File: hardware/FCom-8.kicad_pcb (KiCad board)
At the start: 2 copper layers, 94 x 127 mm, 53 parts, among them J101 USB_C_Receptacle_USB2.0_14P, SW101 SW_DIP_x08, SW102 SW_DIP_x08, SW103 SW_Push_Dual, SW104 SW_DIP_x04, U101 65C02, U102 AS6C1008-55PCN, U103 65C22, U104 74HC245, U105 74HC245, U106 74HC04, U107 74LS08, U108 74LS08, U109 74LS21, U110 MCP23S17_SP

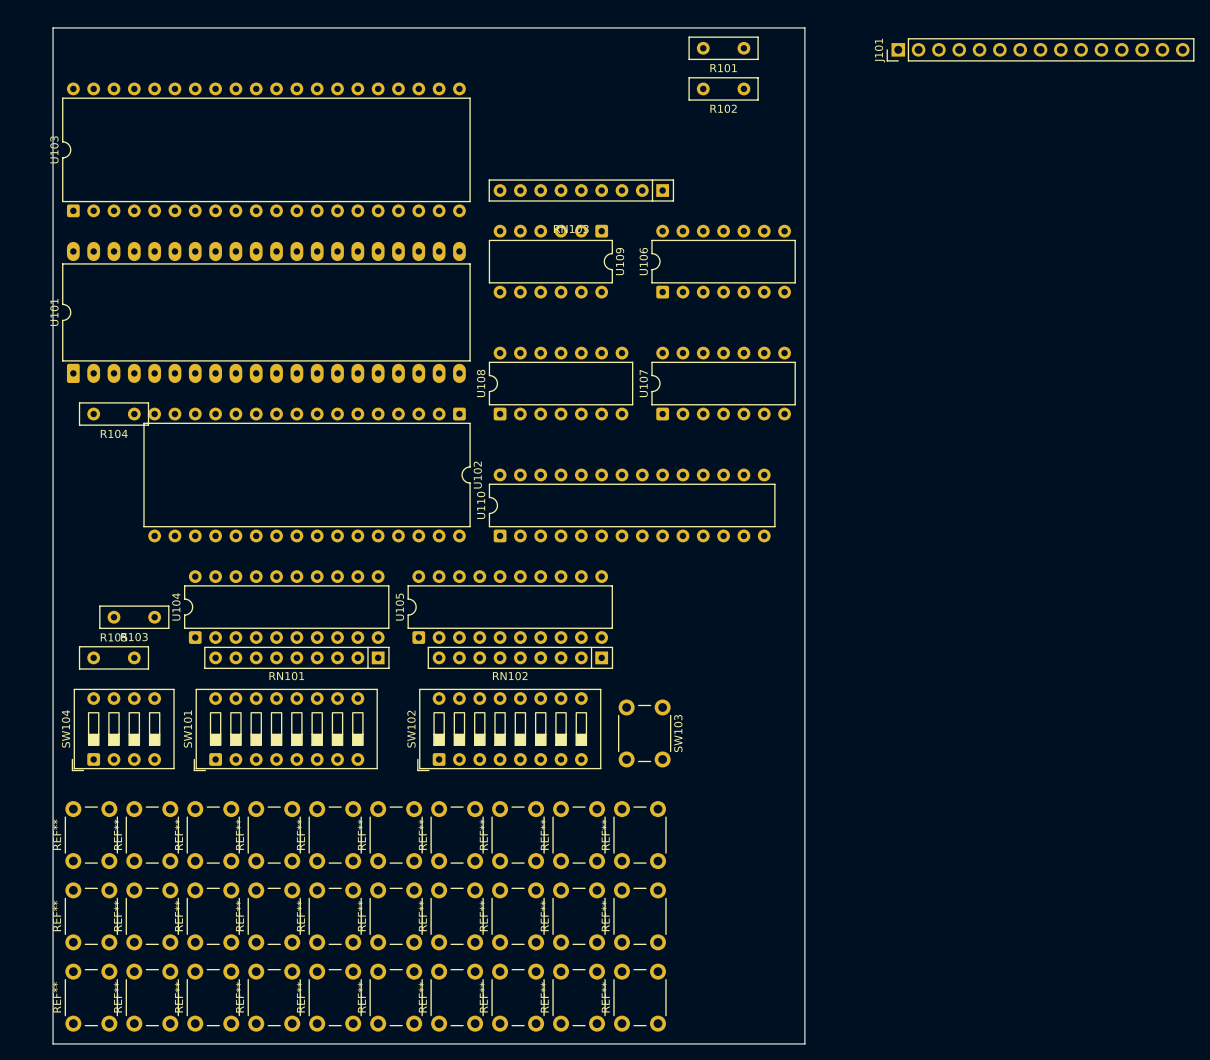
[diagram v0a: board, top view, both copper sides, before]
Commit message: Complete schematics and component placements on board
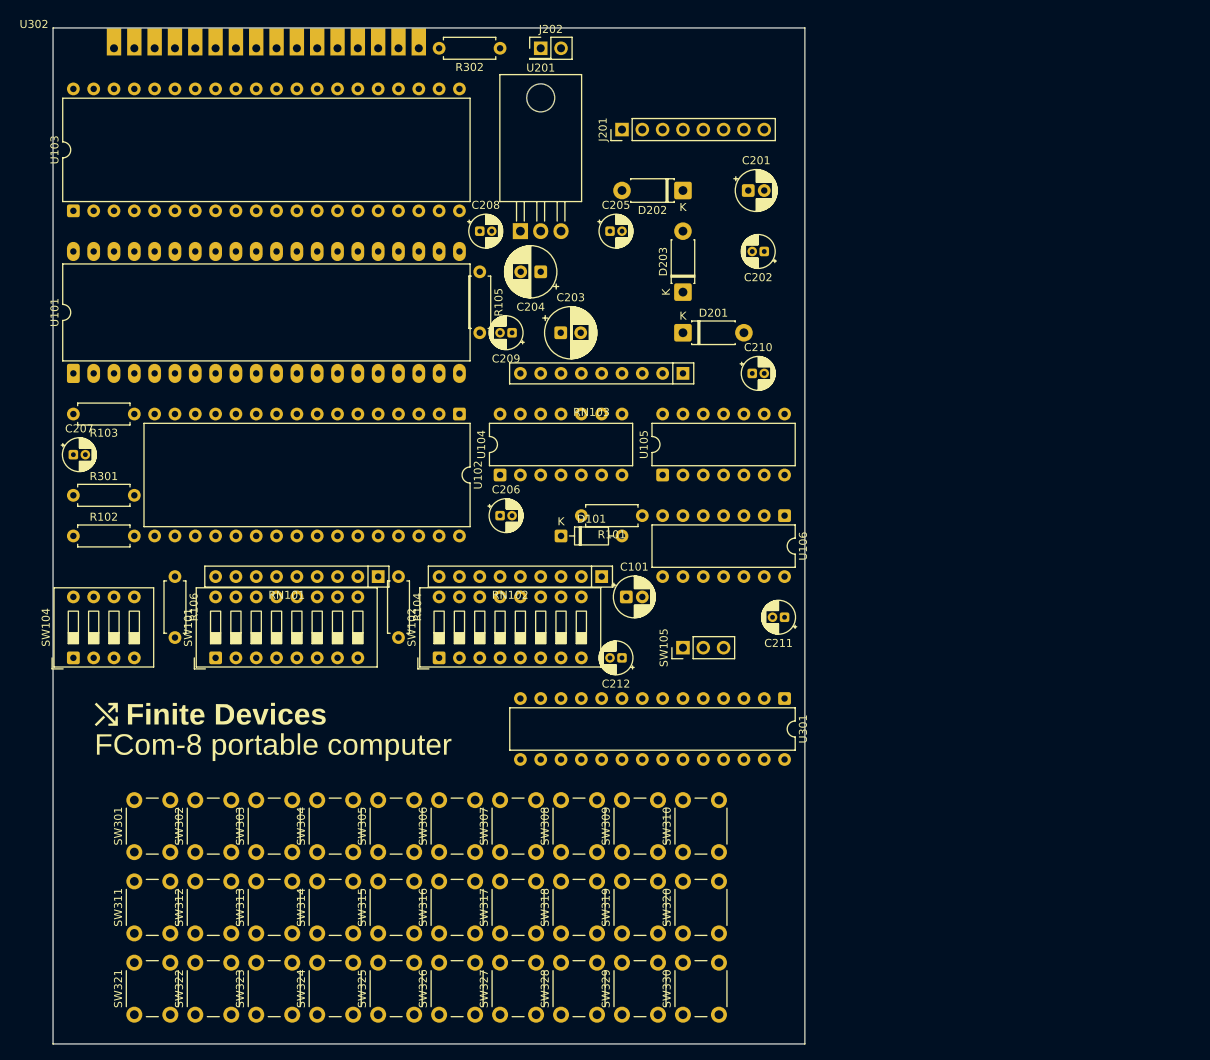
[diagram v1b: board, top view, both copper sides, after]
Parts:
- removed J101: USB_C_Receptacle_USB2.0_14P, Connector_PinHeader_2.54mm:PinHeader_1x15_P2.54mm_Vertical
- removed the R102 at (137.2, 33.0)
- removed the R103 at (63.5, 99.1)
- removed REF** (x30): SW_PUSH_6mm, Button_Switch_THT:SW_PUSH_6mm
- removed SW103: SW_Push_Dual, Button_Switch_THT:SW_PUSH_6mm_H5mm
- removed U107, U108: 74LS08, Package_DIP:DIP-14_W7.62mm
- removed U109: 74LS21, Package_DIP:DIP-12_W7.62mm
- removed U110: MCP23S17_SP, Package_DIP:DIP-28_W7.62mm
- added C101: 4.7u, Capacitor_THT:CP_Radial_D5.0mm_P2.00mm, F.Cu at (122.5, 96.5)
- added C201: 10u, Capacitor_THT:CP_Radial_D5.0mm_P2.00mm, F.Cu at (137.7, 45.7)
- added C202: 0.1u, Capacitor_THT:CP_Radial_D4.0mm_P1.50mm, F.Cu at (139.7, 53.3)
- added C203: 100u, Capacitor_THT:CP_Radial_D6.3mm_P2.50mm, F.Cu at (114.3, 63.5)
- added C204: 100u, Capacitor_THT:CP_Radial_D6.3mm_P2.50mm, F.Cu at (111.8, 55.9)
- added C205: 0.1u, Capacitor_THT:CP_Radial_D4.0mm_P1.50mm, F.Cu at (120.4, 50.8)
- added C206: 0.1u, Capacitor_THT:CP_Radial_D4.0mm_P1.50mm, F.Cu at (106.7, 86.4)
- added C207: 0.1u, Capacitor_THT:CP_Radial_D4.0mm_P1.50mm, F.Cu at (53.3, 78.7)
- added C208: 0.1u, Capacitor_THT:CP_Radial_D4.0mm_P1.50mm, F.Cu at (104.1, 50.8)
- added C209: 0.1u, Capacitor_THT:CP_Radial_D4.0mm_P1.50mm, F.Cu at (108.2, 63.5)
- added C210: 0.1u, Capacitor_THT:CP_Radial_D4.0mm_P1.50mm, F.Cu at (138.2, 68.6)
- added C211: 0.1u, Capacitor_THT:CP_Radial_D4.0mm_P1.50mm, F.Cu at (142.2, 99.1)
- added C212: 0.1u, Capacitor_THT:CP_Radial_D4.0mm_P1.50mm, F.Cu at (121.9, 104.1)
- added D101: 1N4148, Diode_THT:D_DO-35_SOD27_P7.62mm_Horizontal, F.Cu at (114.3, 88.9)
- added D201: D_Schottky, Diode_THT:D_DO-41_SOD81_P7.62mm_Horizontal, F.Cu at (129.5, 63.5)
- added D202: D_Schottky, Diode_THT:D_DO-41_SOD81_P7.62mm_Horizontal, F.Cu at (129.5, 45.7)
- added D203: D_Schottky, Diode_THT:D_DO-41_SOD81_P7.62mm_Horizontal, F.Cu at (129.5, 58.4)
- added G***: LOGO, Components:Badge, F.Cu at (78.7, 113.0)
- added J201: 4090 USB-C, Connector_PinHeader_2.54mm:PinHeader_1x08_P2.54mm_Vertical, F.Cu at (121.9, 38.1)
- added J202: 9V battery, Connector_PinHeader_2.54mm:PinHeader_2x01_P2.54mm_Vertical, F.Cu at (111.8, 27.9)
- added R104: 10k, Resistor_THT:R_Axial_DIN0207_L6.3mm_D2.5mm_P7.62mm_Horizontal, F.Cu at (94.0, 94.0)
- added R105: 10k, Resistor_THT:R_Axial_DIN0207_L6.3mm_D2.5mm_P7.62mm_Horizontal, F.Cu at (104.1, 55.9)
- added R106: 10k, Resistor_THT:R_Axial_DIN0207_L6.3mm_D2.5mm_P7.62mm_Horizontal, F.Cu at (66.0, 94.0)
- added R301: 10k, Resistor_THT:R_Axial_DIN0207_L6.3mm_D2.5mm_P7.62mm_Horizontal, F.Cu at (53.3, 83.8)
- added R302: 1.2k, Resistor_THT:R_Axial_DIN0207_L6.3mm_D2.5mm_P7.62mm_Horizontal, F.Cu at (106.7, 27.9)
- added SW105: G19AP, Connector_PinHeader_2.54mm:PinHeader_1x03_P2.54mm_Vertical, F.Cu at (129.5, 102.9)
- added SW301: Q/1/STOP, Button_Switch_THT:SW_PUSH_6mm, F.Cu at (61.0, 128.4)
- added SW302: W/2/CH0, Button_Switch_THT:SW_PUSH_6mm, F.Cu at (68.6, 128.4)
- added SW303: E/3/CH1, Button_Switch_THT:SW_PUSH_6mm, F.Cu at (76.2, 128.4)
- added SW304: R/4/CH2, Button_Switch_THT:SW_PUSH_6mm, F.Cu at (83.8, 128.4)
- added SW305: T/5/CH3, Button_Switch_THT:SW_PUSH_6mm, F.Cu at (91.4, 128.4)
- added SW306: Y/6/_, Button_Switch_THT:SW_PUSH_6mm, F.Cu at (99.1, 128.4)
- added SW307: U/7/-, Button_Switch_THT:SW_PUSH_6mm, F.Cu at (106.7, 128.4)
- added SW308: I/8/+, Button_Switch_THT:SW_PUSH_6mm, F.Cu at (114.3, 128.4)
- added SW309: O/9/=, Button_Switch_THT:SW_PUSH_6mm, F.Cu at (121.9, 128.4)
- added SW310: P/0, Button_Switch_THT:SW_PUSH_6mm, F.Cu at (129.5, 128.4)
- added SW311: A/!/`, Button_Switch_THT:SW_PUSH_6mm, F.Cu at (61.0, 138.6)
- added SW312: S/"/CH4, Button_Switch_THT:SW_PUSH_6mm, F.Cu at (68.6, 138.6)
- added SW313: D/$/CH5, Button_Switch_THT:SW_PUSH_6mm, F.Cu at (76.2, 138.6)
- added SW314: F/%/CH6, Button_Switch_THT:SW_PUSH_6mm, F.Cu at (83.8, 138.6)
- added SW315: G/^/CH7, Button_Switch_THT:SW_PUSH_6mm, F.Cu at (91.4, 138.6)
- added SW316: H/&/{, Button_Switch_THT:SW_PUSH_6mm, F.Cu at (99.1, 138.6)
- added SW317: J/*/}, Button_Switch_THT:SW_PUSH_6mm, F.Cu at (106.7, 138.6)
- added SW318: K/(/[, Button_Switch_THT:SW_PUSH_6mm, F.Cu at (114.3, 138.6)
- added SW319: L/)/], Button_Switch_THT:SW_PUSH_6mm, F.Cu at (121.9, 138.6)
- added SW320: BKSP/DEL, Button_Switch_THT:SW_PUSH_6mm, F.Cu at (129.5, 138.6)
- added SW321: SHIFT, Button_Switch_THT:SW_PUSH_6mm, F.Cu at (61.0, 148.7)
- added SW322: Z/\/|, Button_Switch_THT:SW_PUSH_6mm, F.Cu at (68.6, 148.7)
- added SW323: X/;/:, Button_Switch_THT:SW_PUSH_6mm, F.Cu at (76.2, 148.7)
- added SW324: C/'/@, Button_Switch_THT:SW_PUSH_6mm, F.Cu at (83.8, 148.7)
- added SW325: V/#/~, Button_Switch_THT:SW_PUSH_6mm, F.Cu at (91.4, 148.7)
- added SW326: B/,/<, Button_Switch_THT:SW_PUSH_6mm, F.Cu at (99.1, 148.7)
- added SW327: N/./>, Button_Switch_THT:SW_PUSH_6mm, F.Cu at (106.7, 148.7)
- added SW328: M///?, Button_Switch_THT:SW_PUSH_6mm, F.Cu at (114.3, 148.7)
- added SW329: SYM, Button_Switch_THT:SW_PUSH_6mm, F.Cu at (121.9, 148.7)
- added SW330: SPC/ENT, Button_Switch_THT:SW_PUSH_6mm, F.Cu at (129.5, 148.7)
- added U201: LM1117T-5.0, Package_TO_SOT_THT:TO-220-3_Horizontal_TabDown, F.Cu at (109.2, 50.8)
- added U301: MCP23S17_SP, Package_DIP:DIP-28_W7.62mm, F.Cu at (142.2, 109.2)
- added U302: NHD-0420DZ-FL-YBW, Components:NHD-0420DZ-FL-YBW, F.Cu at (48.4, 25.4)
- R101: value 5.1k -> 10k; footprint Resistor_THT:R_Box_L8.4mm_W2.5mm_P5.08mm -> Resistor_THT:R_Axial_DIN0207_L6.3mm_D2.5mm_P7.62mm_Horizontal
- R102: renamed from R105; footprint Resistor_THT:R_Box_L8.4mm_W2.5mm_P5.08mm -> Resistor_THT:R_Axial_DIN0207_L6.3mm_D2.5mm_P7.62mm_Horizontal
- R103: renamed from R104; footprint Resistor_THT:R_Box_L8.4mm_W2.5mm_P5.08mm -> Resistor_THT:R_Axial_DIN0207_L6.3mm_D2.5mm_P7.62mm_Horizontal
- U104: value 74HC245 -> 74LS04; footprint Package_DIP:DIP-20_W7.62mm -> Package_DIP:DIP-14_W7.62mm
- U105: value 74HC245 -> 74LS08; footprint Package_DIP:DIP-20_W7.62mm -> Package_DIP:DIP-14_W7.62mm
- U106: value 74HC04 -> 74LS21
- moved R101 59.8 mm to (124.5, 86.4)
- moved U104 43.2 mm to (106.7, 81.3)
- moved U105 36.6 mm to (127.0, 81.3)
- moved U106 31.8 mm to (142.2, 86.4), turned to -90 degrees
- moved RN103 23.0 mm to (129.5, 68.6)
- moved R102 15.5 mm to (53.3, 88.9)
- moved SW104 13.0 mm to (53.3, 104.1)
- moved SW101 12.7 mm to (71.1, 104.1)
- moved SW102 12.7 mm to (99.1, 104.1)
- moved RN101 10.2 mm to (91.4, 94.0)
- moved RN102 10.2 mm to (119.4, 94.0)
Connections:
- R101 pad 1: Net-(J101-CC1) -> GND
- R101 pad 2: GND -> ~{RAM_CS}
- RN101 pad 2: Net-(RN101-R1) -> /A7
- RN101 pad 3: Net-(RN101-R2) -> /A6
- RN101 pad 4: Net-(RN101-R3) -> /A5
- RN101 pad 5: Net-(RN101-R4) -> /A4
- RN101 pad 6: Net-(RN101-R5) -> /A3
- RN101 pad 7: Net-(RN101-R6) -> /A2
- RN101 pad 8: Net-(RN101-R7) -> /A1
- RN101 pad 9: Net-(RN101-R8) -> /A0
- RN102 pad 2: Net-(RN102-R1) -> /D7
- RN102 pad 3: Net-(RN102-R2) -> /D6
- RN102 pad 4: Net-(RN102-R3) -> /D5
- RN102 pad 5: Net-(RN102-R4) -> /D4
- RN102 pad 6: Net-(RN102-R5) -> /D3
- RN102 pad 7: Net-(RN102-R6) -> /D2
- RN102 pad 8: Net-(RN102-R7) -> /D1
- RN102 pad 9: Net-(RN102-R8) -> /D0
- RN103 pad 1: VCC -> +5V
- SW101 pad 1: VCC -> VBS
- SW101 pad 10: Net-(RN101-R2) -> /A6
- SW101 pad 11: Net-(RN101-R3) -> /A5
- SW101 pad 12: Net-(RN101-R4) -> /A4
- SW101 pad 13: Net-(RN101-R5) -> /A3
- SW101 pad 14: Net-(RN101-R6) -> /A2
- SW101 pad 15: Net-(RN101-R7) -> /A1
- SW101 pad 16: Net-(RN101-R8) -> /A0
- SW101 pad 2: VCC -> VBS
- SW101 pad 3: VCC -> VBS
- SW101 pad 4: VCC -> VBS
- SW101 pad 5: VCC -> VBS
- SW101 pad 6: VCC -> VBS
- SW101 pad 7: VCC -> VBS
- SW101 pad 8: VCC -> VBS
- SW101 pad 9: Net-(RN101-R1) -> /A7
- SW102 pad 1: VCC -> VBS
- SW102 pad 10: Net-(RN102-R2) -> /D6
- SW102 pad 11: Net-(RN102-R3) -> /D5
- SW102 pad 12: Net-(RN102-R4) -> /D4
- SW102 pad 13: Net-(RN102-R5) -> /D3
- SW102 pad 14: Net-(RN102-R6) -> /D2
- SW102 pad 15: Net-(RN102-R7) -> /D1
- SW102 pad 16: Net-(RN102-R8) -> /D0
- SW102 pad 2: VCC -> VBS
- SW102 pad 3: VCC -> VBS
- SW102 pad 4: VCC -> VBS
- SW102 pad 5: VCC -> VBS
- SW102 pad 6: VCC -> VBS
- SW102 pad 7: VCC -> VBS
- SW102 pad 8: VCC -> VBS
- SW102 pad 9: Net-(RN102-R1) -> /D7
- SW104 pad 1: VCC -> +5V
- SW104 pad 4: VCC -> unconnected-(SW104-Pad4)
- SW104 pad 5: ~{RESET} -> unconnected-(SW104-Pad5)
- U101 pad 36: ~{RESET} -> VCC
- U101 pad 40: ~{RESET} -> VCC
- U102 pad 22: Net-(U102-~{CS1}/~{CE1}) -> ~{RAM_CS}
- U102 pad 29: Net-(U102-~{WE}) -> ~{WE}
- U102 pad 30: Net-(U102-CS2/CE2) -> PHI2O
- U103 pad 10: unconnected-(U103-PB0-Pad10) -> KB_SO
- U103 pad 11: unconnected-(U103-PB1-Pad11) -> KB_SI
- U103 pad 12: unconnected-(U103-PB2-Pad12) -> KB_SCK
- U103 pad 13: unconnected-(U103-PB3-Pad13) -> ~{KB_CS}
- U103 pad 2: unconnected-(U103-PA0-Pad2) -> DISP_D0
- U103 pad 3: unconnected-(U103-PA1-Pad3) -> DISP_D1
- U103 pad 4: unconnected-(U103-PA2-Pad4) -> DISP_D2
- U103 pad 40: unconnected-(U103-CA1-Pad40) -> KB_INT
- U103 pad 5: unconnected-(U103-PA3-Pad5) -> DISP_D3
- U103 pad 6: unconnected-(U103-PA4-Pad6) -> DISP_D4
- U103 pad 7: unconnected-(U103-PA5-Pad7) -> DISP_D5
- U103 pad 8: unconnected-(U103-PA6-Pad8) -> DISP_D6
- U103 pad 9: unconnected-(U103-PA7-Pad9) -> DISP_D7
- U104 pad 1: VCC -> ~{WE}
- U104 pad 10: GND -> unconnected-(U104-Pad10)
- U104 pad 11: /A7 -> GND
- U104 pad 12: /A6 -> unconnected-(U104-Pad12)
- U104 pad 13: /A5 -> GND
- U104 pad 14: /A4 -> VCC
- U104 pad 2: Net-(RN101-R8) -> Net-(U102-~{OE})
- U104 pad 3: Net-(RN101-R7) -> /A8
- U104 pad 4: Net-(RN101-R6) -> Net-(U104-Pad4)
- U104 pad 5: Net-(RN101-R5) -> ~{RAM_CS}
- U104 pad 6: Net-(RN101-R4) -> ~{VIA_CS}
- U104 pad 7: Net-(RN101-R3) -> GND
- U104 pad 8: Net-(RN101-R2) -> unconnected-(U104-Pad8)
- U104 pad 9: Net-(RN101-R1) -> GND
- U105 pad 1: VCC -> Net-(U105-Pad1)
- U105 pad 11: /D7 -> unconnected-(U105-Pad11)
- U105 pad 12: /D6 -> GND
- U105 pad 13: /D5 -> GND
- U105 pad 14: /D4 -> VCC
- U105 pad 2: Net-(RN102-R8) -> Net-(U105-Pad2)
- U105 pad 3: Net-(RN102-R7) -> ~{RAM_CS}
- U105 pad 4: Net-(RN102-R6) -> GND
- U105 pad 5: Net-(RN102-R5) -> GND
- U105 pad 6: Net-(RN102-R4) -> unconnected-(U105-Pad6)
- U105 pad 7: Net-(RN102-R3) -> GND
- U105 pad 8: Net-(RN102-R2) -> unconnected-(U105-Pad8)
- U105 pad 9: Net-(RN102-R1) -> GND
- U106 pad 1: ~{RESET} -> Net-(U104-Pad4)
- U106 pad 10: Net-(U102-~{OE}) -> /A9
- U106 pad 11: Net-(U102-~{WE}) -> (no net)
- U106 pad 12: Net-(U106-Pad12) -> /A14
- U106 pad 13: /A8 -> /A15
- U106 pad 2: Net-(U106-Pad2) -> /A13
- U106 pad 3: Net-(U106-Pad3) -> (no net)
- U106 pad 4: Net-(U102-CS2/CE2) -> /A11
- U106 pad 5: Net-(U106-Pad5) -> /A10
- U106 pad 6: Net-(U106-Pad6) -> Net-(U105-Pad1)
- U106 pad 8: ~{VIA_CS} -> Net-(U105-Pad2)
- U106 pad 9: ~{RAM_CS} -> /A12
